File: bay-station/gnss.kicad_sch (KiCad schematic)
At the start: 8 parts, among them U10 LIS3MDL, U11 LIS2DH, U9 MAX-M10S

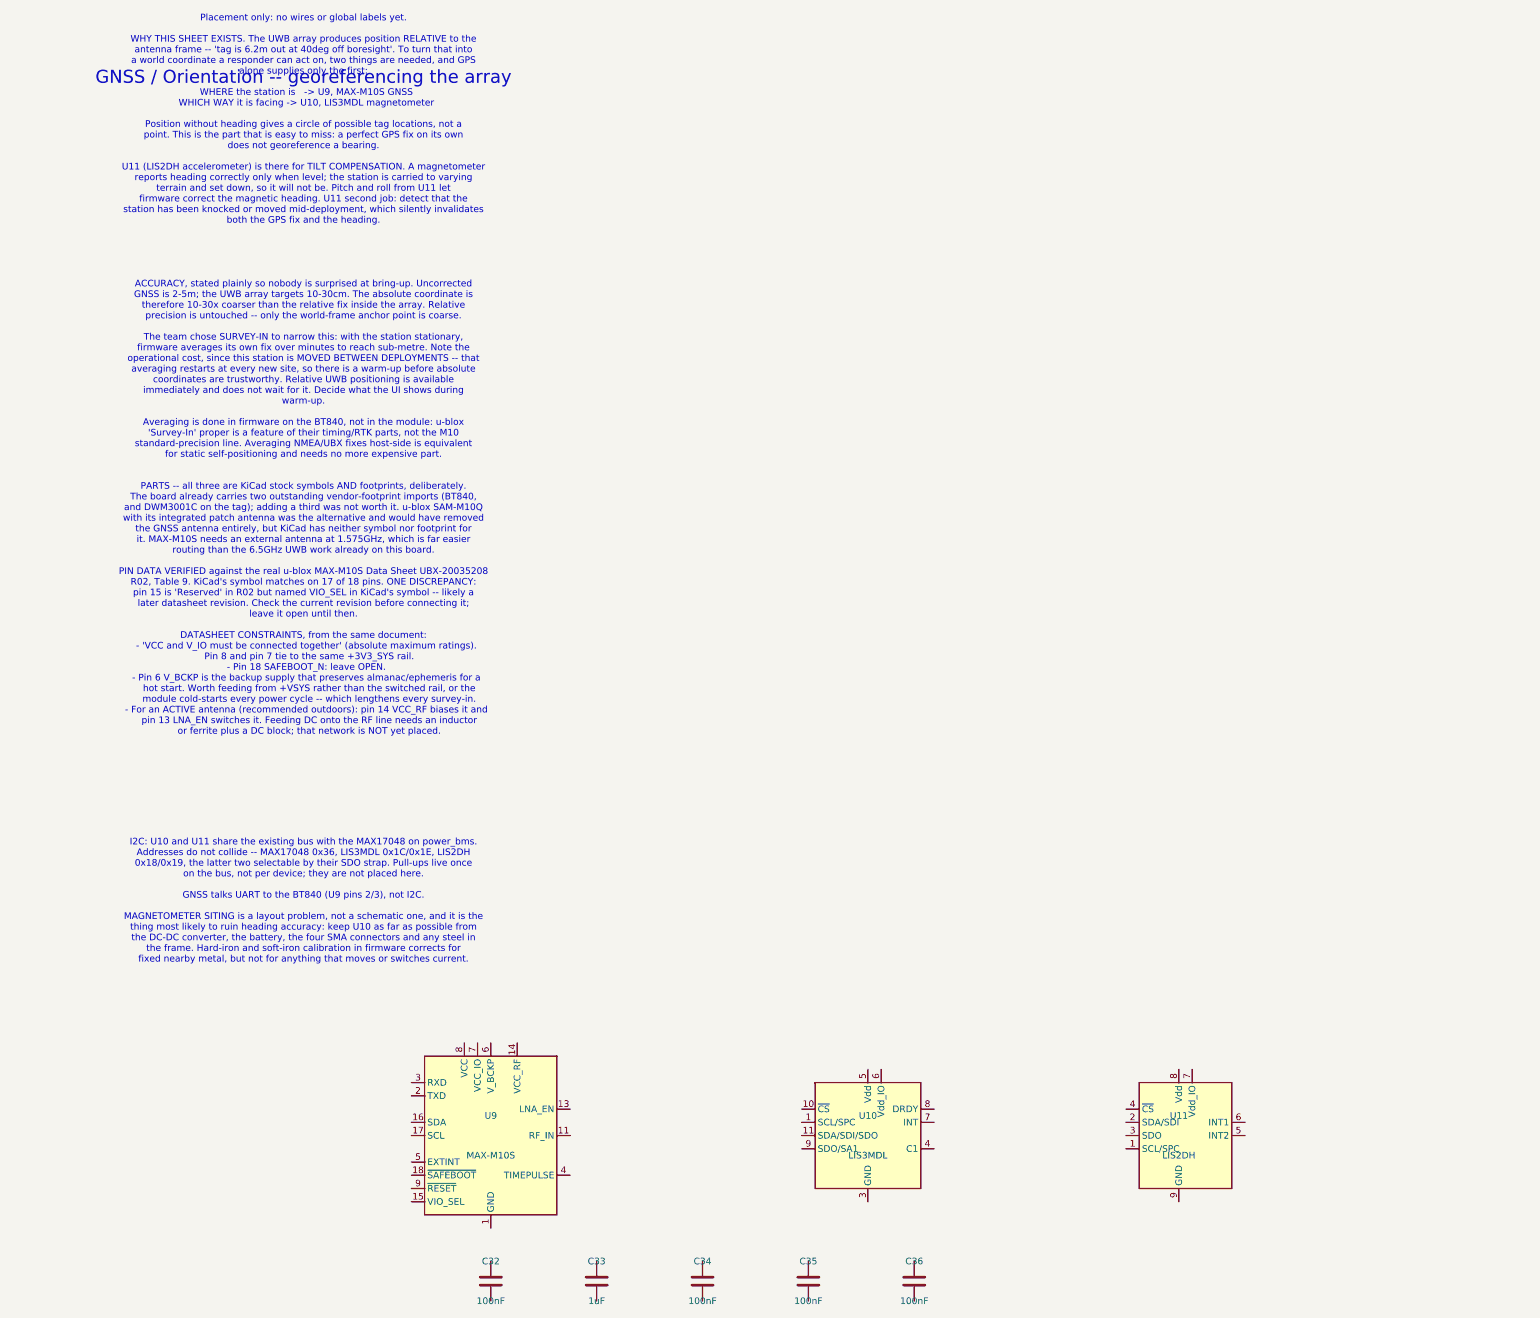
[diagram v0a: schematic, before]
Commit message: Wire up power_bms, regulation and programming_debug; tie off floating grounds
The bay station was built entirely from global labels and power symbols --
zero drawn wires on any sheet. This starts converting the power path to
explicit wiring and connects the grounds that were left floating:

- power_bms: 62 wires; 31 label justifications flipped left->right where
  the labels were mirrored. No symbols added or removed.
- regulation: 11 wires, 3 junctions, 5 GND symbols (#PWR01-05).
- programming_debug: 2 wires, 1 junction, 1 GND symbol (#PWR06).

ERC goes 518 -> 497 violations (494 -> 473 errors), entirely in
pin_not_connected (360 -> 342), power_pin_not_driven (98 -> 96) and
pin_not_driven (36 -> 35). Nothing regressed. The remaining 342
pin_not_connected are the sheets that are still label-only.

Unavoidable churn in this commit: KiCad 10 re-serialized seven sheets from
8.0 format (version 20231120) to 10.0 (20260306) on save -- clock_dist,
connectivity, gnss, indicators, programming_debug, testpoints, uwb_array.
That accounts for most of the diff; those seven have no content change
beyond it. CLAUDE.md asks that the format not be bumped as a side effect,
but it cannot be split out here: kicad-cli sch upgrade serializes
differently from the GUI and leaves ~3700 lines of residual churn, so a
format-only commit would be tidier in shape and no more honest. Four
sheets were already on 10.0 format before this commit.

Co-Authored-By: Claude Opus 5 (1M context) <noreply@anthropic.com>
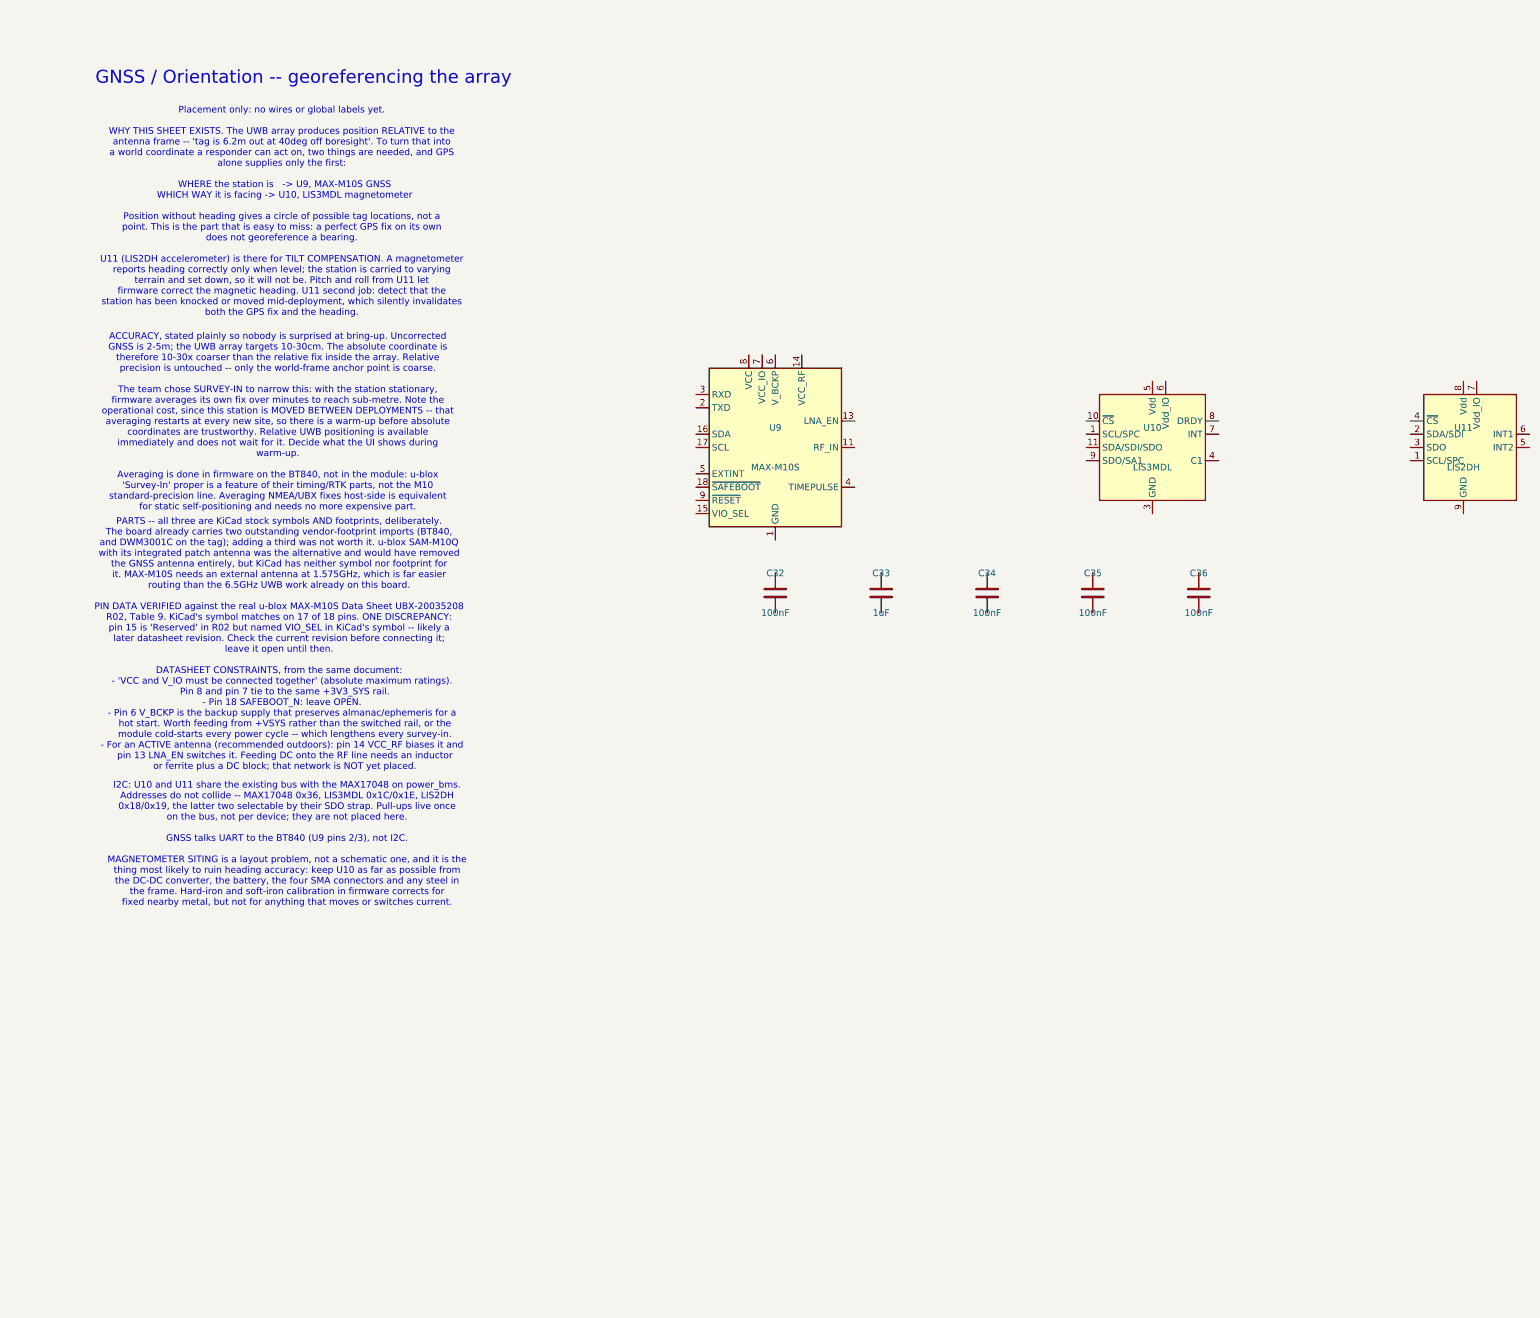
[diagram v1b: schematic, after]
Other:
- moved on the sheet: C32, C33, C34, C35, C36, U10, U11, U9
